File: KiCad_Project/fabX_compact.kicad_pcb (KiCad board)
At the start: 2 copper layers, 62 x 90 mm, 69 parts, among them J1 SolderJumper_2_Open, J2 SolderJumper_2_Open, J3 SolderJumper_2_Open, J4 SolderJumper_2_Open, J5 SolderJumper_2_Open, J6 SolderJumper_2_Open, K2 PCN-105D3MHZ, Q1 2N7002, Q2 DMP3056L-7, Q3 2N7002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

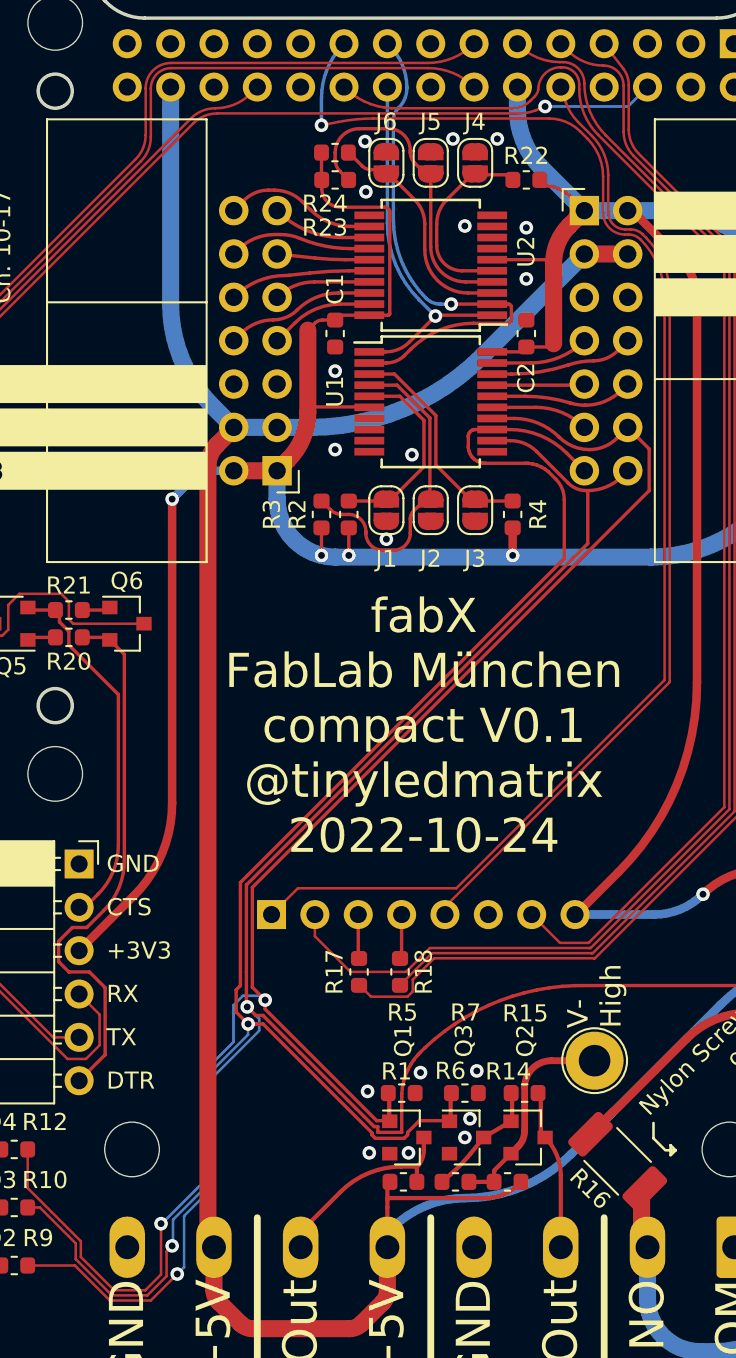
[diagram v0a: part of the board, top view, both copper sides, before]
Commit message: new PCB Version V0.2
Added new Pulddown Rs to PCB
DRC okay
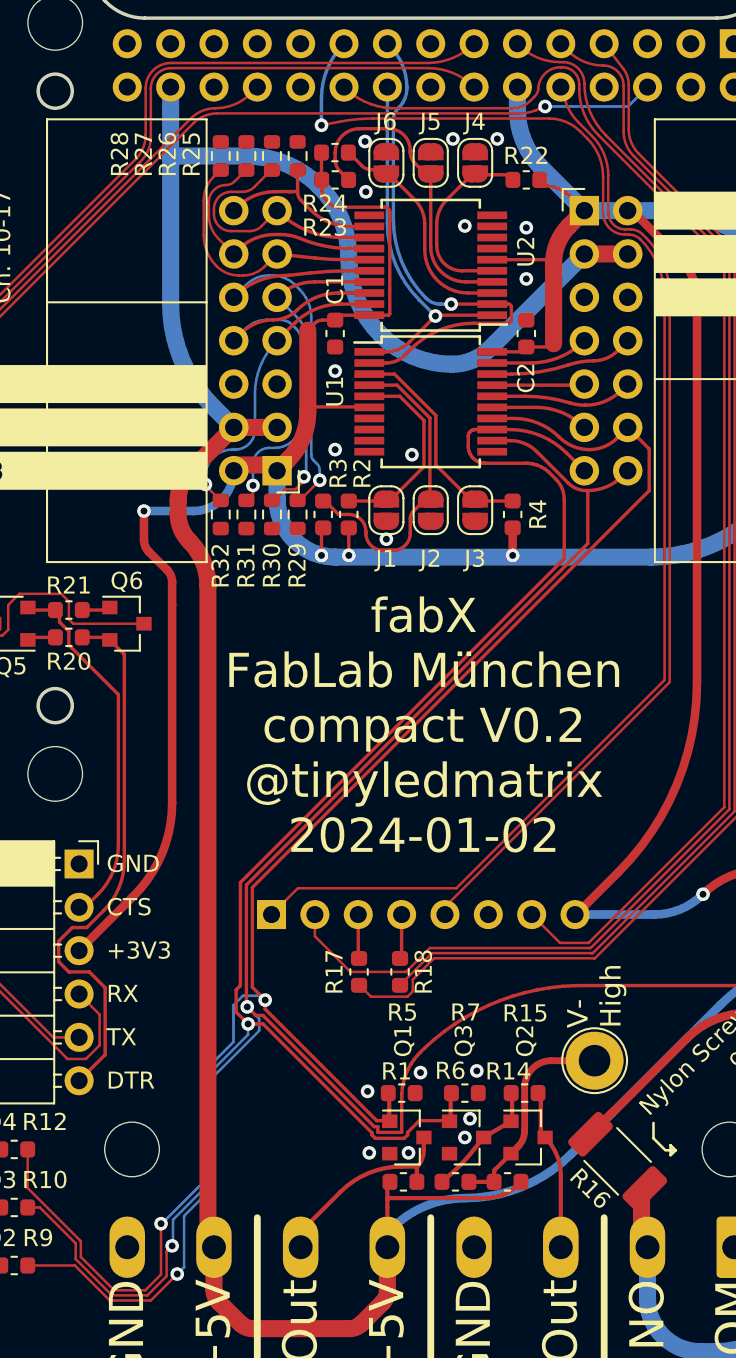
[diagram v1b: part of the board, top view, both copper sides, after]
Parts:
- added R25: 100k, Resistor_SMD:R_0603_1608Metric, F.Cu at (142.1, 78.4)
- added R26: 100k, Resistor_SMD:R_0603_1608Metric, F.Cu at (140.6, 78.4)
- added R27: 100k, Resistor_SMD:R_0603_1608Metric, F.Cu at (139.1, 78.4)
- added R28: 100k, Resistor_SMD:R_0603_1608Metric, F.Cu at (137.6, 78.4)
- added R29: 100k, Resistor_SMD:R_0603_1608Metric, F.Cu at (142.1, 99.4)
- added R30: 100k, Resistor_SMD:R_0603_1608Metric, F.Cu at (140.6, 99.4)
- added R31: 100k, Resistor_SMD:R_0603_1608Metric, F.Cu at (139.1, 99.4)
- added R32: 100k, Resistor_SMD:R_0603_1608Metric, F.Cu at (137.6, 99.4)
- moved R3 0.10 mm to (143.6, 99.4)
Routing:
- net /Ch14: track 8.28 -> 26.1 mm, vias 0 -> 1
- net /Ch16: track 8.71 -> 24.9 mm, vias 0 -> 1
- net /Ch15: track 5.63 -> 19.4 mm, vias 0 -> 1
- net +5V: track 169.0 -> 182.2 mm
- net /Ch17: track 6.11 -> 17.8 mm, vias 0 -> 1
- net /Ch13: track 5.42 -> 15.7 mm
- net /Ch11: track 5.79 -> 15.2 mm
- net /Ch12: track 8.37 -> 15.0 mm
- net +3V3: track 219.6 -> 221.7 mm
- net /Ch10: track 8.95 -> 10.6 mm
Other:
- board text added: "fabX FabLab München compact V0.2 @tinyledmatrix 2024-01-02"
- board text removed: "fabX FabLab München compact V0.1 @tinyledmatrix 2022-10-24"
